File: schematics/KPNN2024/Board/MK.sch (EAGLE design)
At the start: 17 parts

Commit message: добавлены стл корпусных деталей
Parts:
- C1: value (none) -> 100nF
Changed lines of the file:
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@@
 <part name="R5" library="rcl" library_urn="urn:adsk.eagle:library:334" deviceset="R-US_" device="R0603" package3d_urn="urn:adsk.eagle:package:23555/3" value="10k"/>
 <part name="R6" library="rcl" library_urn="urn:adsk.eagle:library:334" deviceset="R-US_" device="R0603" package3d_urn="urn:adsk.eagle:package:23555/3" value="10k"/>
-<part name="C1" library="rcl" library_urn="urn:adsk.eagle:library:334" deviceset="C-EU" device="C0603" package3d_urn="urn:adsk.eagle:package:23616/2"/>
+<part name="C1" library="rcl" library_urn="urn:adsk.eagle:library:334" deviceset="C-EU" device="C0603" package3d_urn="urn:adsk.eagle:package:23616/2" value="100nF"/>
 </parts>
 <sheets>

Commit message: ывавп лыл
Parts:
- renumbered U$20 to SI2302CDS, U$5 to STM

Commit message: Платы вроде готовы
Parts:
- added STATE: (no value), led:LEDCHIPLED_0603
- R1, R2: value 10k -> 2k
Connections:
- net 3V3: no longer BME280.VIN
- net 5V: now also BME280.VIN; no longer STM.5V
- net DIR_DRIVER: now also STM.PA10, U$4.12; no longer STM.PA9, U$4.13
- net GND: now also STATE.C
- net STEP_DRIVER: now also STM.PA9, U$4.13; no longer STM.PA10, U$4.12
- net SWITCH: now also STATE.A
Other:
- moved on the sheet: C1, MICRO_SD, R1, R2, R5, R6, U$2

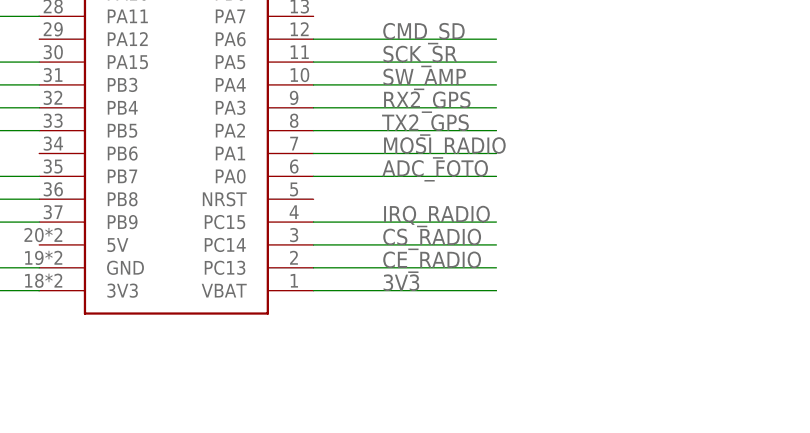
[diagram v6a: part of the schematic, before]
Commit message: поправила платы
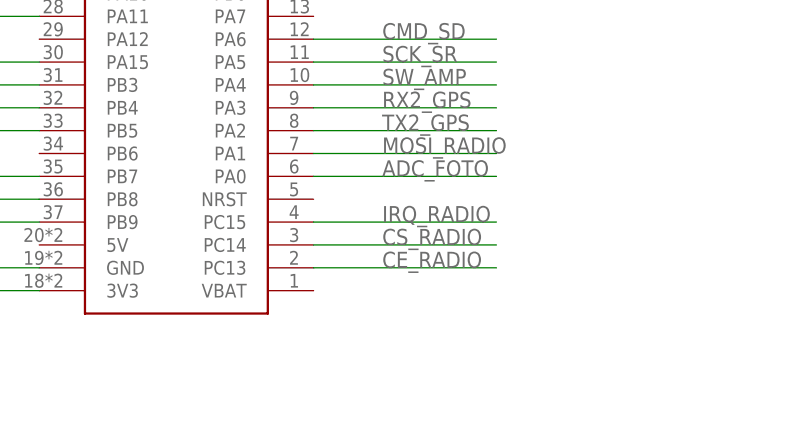
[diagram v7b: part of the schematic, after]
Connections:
- net 3V3: no longer STM.VBAT
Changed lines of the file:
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@@
 <?xml version="1.0" encoding="utf-8"?>
 <!DOCTYPE eagle SYSTEM "eagle.dtd">
-<eagle version="9.6.2">
+<eagle version="9.4.2">
 <drawing>
 <settings>
-<setting alwaysvectorfont="no"/>
+<setting alwaysvectorfont="yes"/>
 <setting verticaltext="up"/>
 </settings>
@@
 </segment>
 <segment>
-<pinref part="STM" gate="G$1" pin="VBAT"/>
-<wire x1="-38.1" y1="38.1" x2="-17.78" y2="38.1" width="0.1524" layer="91"/>
-<label x="-30.48" y="38.1" size="1.778" layer="95"/>
-</segment>
-<segment>

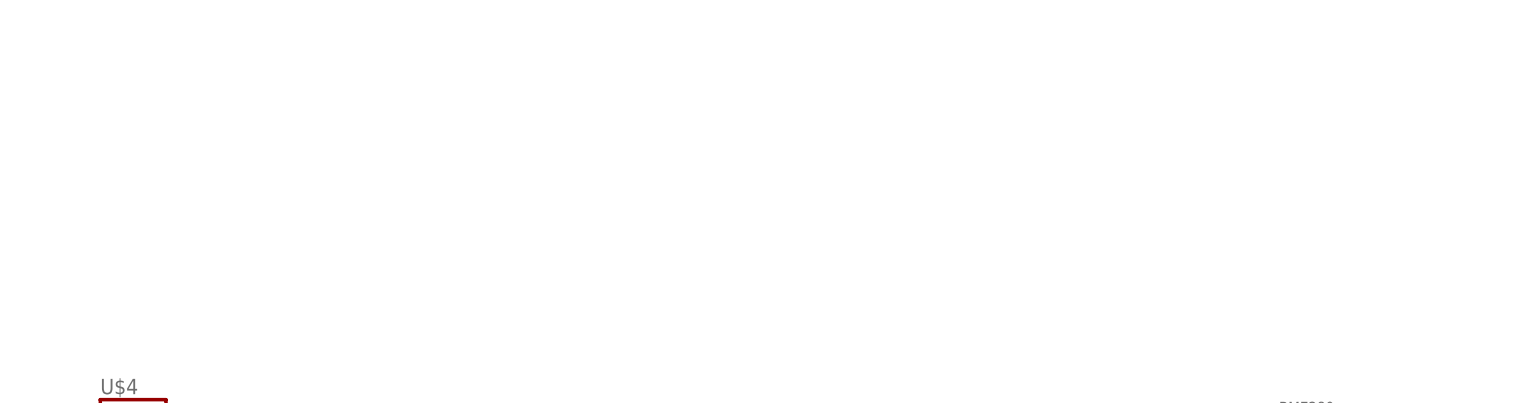
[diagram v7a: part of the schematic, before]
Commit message: Модели поправлены в соответствии с платами
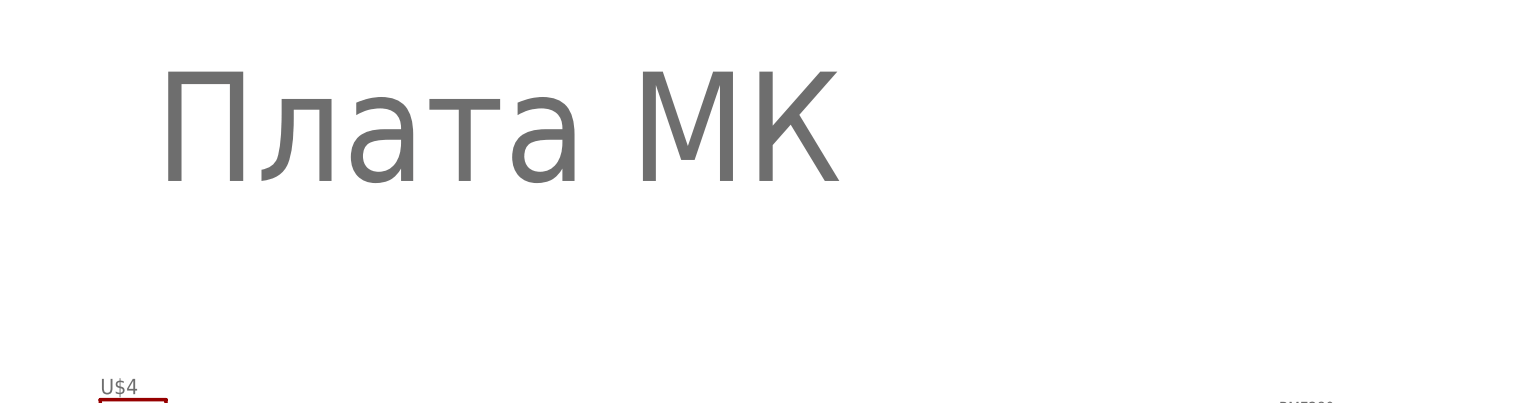
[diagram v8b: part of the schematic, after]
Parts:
- added U$1: Плата МК, UNKNOWN-2024:LOGOPCB-""
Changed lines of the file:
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@@
 <part name="C1" library="rcl" library_urn="urn:adsk.eagle:library:334" deviceset="C-EU" device="C0603" package3d_urn="urn:adsk.eagle:package:23616/2" value="100nF"/>
 <part name="STATE" library="led" library_urn="urn:adsk.eagle:library:259" deviceset="LED" device="CHIPLED_0603" package3d_urn="urn:adsk.eagle:package:15822/2"/>
+<part name="U$1" library="UNKNOWN-2024" deviceset="LOGO" device="PCB-&quot;&quot;" value="Плата МК"/>
 </parts>
 <sheets>
@@
 <attribute name="VALUE" x="155.575" y="46.228" size="1.778" layer="96" rot="R90"/>
 </instance>
+<instance part="U$1" gate="G$1" x="-25.4" y="134.62" smashed="yes">
+<attribute name="VALUE" x="78.74" y="134.62" size="12.7" layer="96"/>
+</instance>
 </instances>
